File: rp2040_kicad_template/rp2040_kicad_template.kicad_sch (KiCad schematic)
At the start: 48 parts

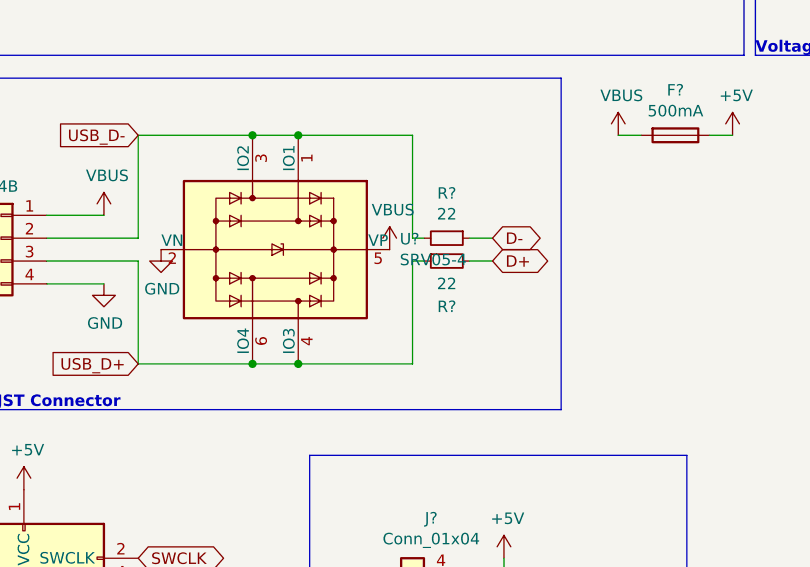
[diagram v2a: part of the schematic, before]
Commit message: Update RP2040 to use 27 ohm resistors
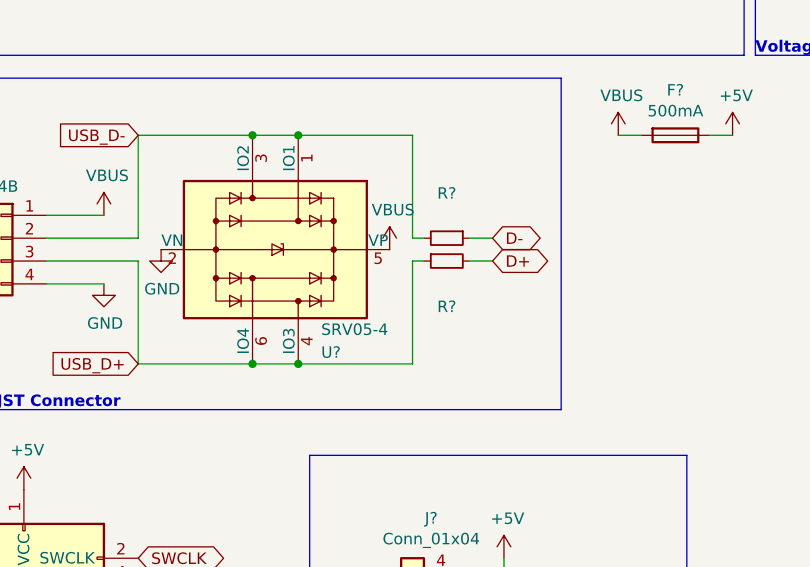
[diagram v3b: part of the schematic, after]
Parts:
- C? (x14), CS?: footprint (none) -> Capacitor_SMD:C_0402_1005Metric
- J?: footprint (none) -> Type-C:USB_C_GCT_USB4085
- R? (x9), RS?: footprint (none) -> Resistor_SMD:R_0402_1005Metric
- R? (x2): value 22 -> (none); footprint (none) -> Resistor_SMD:R_0402_1005Metric
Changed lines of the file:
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@@
     (property "Reference" "R?" (id 0) (at 107.95 34.3916 90))
     (property "Value" "27" (id 1) (at 107.95 36.703 90))
-    (property "Footprint" "" (id 2) (at 107.95 39.37 0)
+    (property "Footprint" "Resistor_SMD:R_0402_1005Metric" (id 2) (at 107.95 39.37 0)
       (effects (font (size 1.27 1.27)) hide)
     )
@@
     (property "Reference" "R?" (id 0) (at 107.95 46.99 90))
     (property "Value" "27" (id 1) (at 107.95 44.45 90))
-    (property "Footprint" "" (id 2) (at 107.95 41.91 0)
+    (property "Footprint" "Resistor_SMD:R_0402_1005Metric" (id 2) (at 107.95 41.91 0)
       (effects (font (size 1.27 1.27)) hide)
     )
@@
     (property "Reference" "R?" (id 0) (at 142.24 36.83 90))
     (property "Value" "10k" (id 1) (at 144.78 36.83 90))
-    (property "Footprint" "" (id 2) (at 147.32 36.83 0)
+    (property "Footprint" "Resistor_SMD:R_0402_1005Metric" (id 2) (at 147.32 36.83 0)
       (effects (font (size 1.27 1.27)) hide)
     )
@@
     (property "Reference" "R?" (id 0) (at 143.51 27.94 90))
     (property "Value" "100" (id 1) (at 143.51 30.48 90))
-    (property "Footprint" "" (id 2) (at 143.51 33.02 0)
+    (property "Footprint" "Resistor_SMD:R_0402_1005Metric" (id 2) (at 143.51 33.02 0)
       (effects (font (size 1.27 1.27)) hide)
     )
@@
     (property "Reference" "R?" (id 0) (at 55.9816 53.34 90))
     (property "Value" "5.1k" (id 1) (at 58.293 53.34 90))
-    (property "Footprint" "" (id 2) (at 60.96 53.34 0)
+    (property "Footprint" "Resistor_SMD:R_0402_1005Metric" (id 2) (at 60.96 53.34 0)
       (effects (font (size 1.27 1.27)) hide)
     )
@@
     (property "Reference" "R?" (id 0) (at 63.6016 53.34 90))
     (property "Value" "5.1k" (id 1) (at 65.913 53.34 90))
-    (property "Footprint" "" (id 2) (at 68.58 53.34 0)
+    (property "Footprint" "Resistor_SMD:R_0402_1005Metric" (id 2) (at 68.58 53.34 0)
       (effects (font (size 1.27 1.27)) hide)
     )
@@
     (in_bom yes) (on_board yes)
     (property "Reference" "R?" (id 0) (at 86.36 95.3516 90))
-    (property "Value" "22" (id 1) (at 86.36 97.663 90))
-    (property "Footprint" "" (id 2) (at 86.36 100.33 0)
+    (property "Value" "" (id 1) (at 86.36 97.663 90))
+    (property "Footprint" "Resistor_SMD:R_0402_1005Metric" (id 2) (at 86.36 100.33 0)
       (effects (font (size 1.27 1.27)) hide)
     )
@@
     (in_bom yes) (on_board yes)
     (property "Reference" "R?" (id 0) (at 86.36 107.95 90))
-    (property "Value" "22" (id 1) (at 86.36 105.41 90))
-    (property "Footprint" "" (id 2) (at 86.36 102.87 0)
+    (property "Value" "" (id 1) (at 86.36 105.41 90))
+    (property "Footprint" "Resistor_SMD:R_0402_1005Metric" (id 2) (at 86.36 102.87 0)
       (effects (font (size 1.27 1.27)) hide)
     )
@@
     (property "Reference" "RS?" (id 0) (at 32.9184 67.31 90))
     (property "Value" "1M" (id 1) (at 30.607 67.31 90))
-    (property "Footprint" "" (id 2) (at 27.94 67.31 0)
+    (property "Footprint" "Resistor_SMD:R_0402_1005Metric" (id 2) (at 27.94 67.31 0)
       (effects (font (size 1.27 1.27)) hide)
     )
@@
       (effects (font (size 1.27 1.27)) (justify left))
     )
-    (property "Footprint" "" (id 2) (at 22.86 67.31 0)
+    (property "Footprint" "Capacitor_SMD:C_0402_1005Metric" (id 2) (at 22.86 67.31 0)
       (effects (font (size 1.27 1.27)) hide)
     )
@@
   (symbol (lib_id "Power_Protection:SRV05-4") (at 67.31 101.6 270) (unit 1)
     (in_bom yes) (on_board yes)
-    (property "Reference" "U?" (id 0) (at 81.1276 100.4316 90)
-      (effects (font (size 1.27 1.27)) (justify left))
-    )
-    (property "Value" "SRV05-4" (id 1) (at 81.1276 102.743 90)
+    (property "Reference" "U?" (id 0) (at 72.39 113.03 90)
+      (effects (font (size 1.27 1.27)) (justify left))
+    )
+    (property "Value" "SRV05-4" (id 1) (at 72.39 110.49 90)
       (effects (font (size 1.27 1.27)) (justify left))
     )
@@
     (property "Reference" "R?" (id 0) (at 208.28 52.07 90))
     (property "Value" "10K" (id 1) (at 210.82 52.07 90))
-    (property "Footprint" "" (id 2) (at 213.36 52.07 0)
+    (property "Footprint" "Resistor_SMD:R_0402_1005Metric" (id 2) (at 213.36 52.07 0)
       (effects (font (size 1.27 1.27)) hide)
     )
@@
     (property "Reference" "R?" (id 0) (at 204.47 83.82 90))
     (property "Value" "1k" (id 1) (at 204.47 86.36 90))
-    (property "Footprint" "" (id 2) (at 204.47 88.9 0)
+    (property "Footprint" "Resistor_SMD:R_0402_1005Metric" (id 2) (at 204.47 88.9 0)
       (effects (font (size 1.27 1.27)) hide)
     )
@@
       (effects (font (size 1.27 1.27)) (justify left))
     )
-    (property "Footprint" "" (id 2) (at 184.15 81.28 0)
+    (property "Footprint" "Capacitor_SMD:C_0402_1005Metric" (id 2) (at 184.15 81.28 0)
       (effects (font (size 1.27 1.27)) hide)
     )
@@
       (effects (font (size 1.27 1.27)) (justify left))
     )
-    (property "Footprint" "" (id 2) (at 184.15 88.9 0)
+    (property "Footprint" "Capacitor_SMD:C_0402_1005Metric" (id 2) (at 184.15 88.9 0)
       (effects (font (size 1.27 1.27)) hide)
     )
@@
       (effects (font (size 1.27 1.27)) (justify left))
     )
-    (property "Footprint" "" (id 2) (at 262.89 22.86 0)
+    (property "Footprint" "Capacitor_SMD:C_0402_1005Metric" (id 2) (at 262.89 22.86 0)
       (effects (font (size 1.27 1.27)) hide)
     )
@@
       (effects (font (size 1.27 1.27)) (justify left))
     )
-    (property "Footprint" "" (id 2) (at 273.05 22.86 0)
+    (property "Footprint" "Capacitor_SMD:C_0402_1005Metric" (id 2) (at 273.05 22.86 0)
       (effects (font (size 1.27 1.27)) hide)
     )
@@
       (effects (font (size 1.27 1.27)) (justify left))
     )
-    (property "Footprint" "" (id 2) (at 283.21 22.86 0)
+    (property "Footprint" "Capacitor_SMD:C_0402_1005Metric" (id 2) (at 283.21 22.86 0)
       (effects (font (size 1.27 1.27)) hide)
     )
@@
       (effects (font (size 1.27 1.27)) (justify left))
     )
-    (property "Footprint" "" (id 2) (at 293.37 22.86 0)
+    (property "Footprint" "Capacitor_SMD:C_0402_1005Metric" (id 2) (at 293.37 22.86 0)
       (effects (font (size 1.27 1.27)) hide)
     )
@@
       (effects (font (size 1.27 1.27)) (justify left))
     )
-    (property "Footprint" "" (id 2) (at 303.53 22.86 0)
+    (property "Footprint" "Capacitor_SMD:C_0402_1005Metric" (id 2) (at 303.53 22.86 0)
       (effects (font (size 1.27 1.27)) hide)
     )
@@
       (effects (font (size 1.27 1.27)) (justify left))
     )
-    (property "Footprint" "" (id 2) (at 313.69 22.86 0)
+    (property "Footprint" "Capacitor_SMD:C_0402_1005Metric" (id 2) (at 313.69 22.86 0)
       (effects (font (size 1.27 1.27)) hide)
     )
@@
       (effects (font (size 1.27 1.27)) (justify left))
     )
-    (property "Footprint" "" (id 2) (at 323.85 22.86 0)
+    (property "Footprint" "Capacitor_SMD:C_0402_1005Metric" (id 2) (at 323.85 22.86 0)
       (effects (font (size 1.27 1.27)) hide)
     )
@@
       (effects (font (size 1.27 1.27)) (justify left))
     )
-    (property "Footprint" "" (id 2) (at 334.01 22.86 0)
+    (property "Footprint" "Capacitor_SMD:C_0402_1005Metric" (id 2) (at 334.01 22.86 0)
       (effects (font (size 1.27 1.27)) hide)
     )
@@
       (effects (font (size 1.27 1.27)) (justify left))
     )
-    (property "Footprint" "" (id 2) (at 344.17 22.86 0)
+    (property "Footprint" "Capacitor_SMD:C_0402_1005Metric" (id 2) (at 344.17 22.86 0)
       (effects (font (size 1.27 1.27)) hide)
     )
@@
       (effects (font (size 1.27 1.27)) (justify left))
     )
-    (property "Footprint" "" (id 2) (at 179.07 22.86 0)
+    (property "Footprint" "Capacitor_SMD:C_0402_1005Metric" (id 2) (at 179.07 22.86 0)
       (effects (font (size 1.27 1.27)) hide)
     )
@@
       (effects (font (size 1.27 1.27)) (justify left))
     )
-    (property "Footprint" "" (id 2) (at 189.23 22.86 0)
+    (property "Footprint" "Capacitor_SMD:C_0402_1005Metric" (id 2) (at 189.23 22.86 0)
       (effects (font (size 1.27 1.27)) hide)
     )
@@
       (effects (font (size 1.27 1.27)) (justify left))
     )
-    (property "Footprint" "" (id 2) (at 240.03 170.18 0)
+    (property "Footprint" "Capacitor_SMD:C_0402_1005Metric" (id 2) (at 240.03 170.18 0)
       (effects (font (size 1.27 1.27)) hide)
     )
@@
     (property "Reference" "J?" (id 0) (at 33.02 17.8902 0))
     (property "Value" "USB_C_Receptacle_USB2.0" (id 1) (at 33.02 20.4271 0))
-    (property "Footprint" "" (id 2) (at 36.83 39.37 0)
+    (property "Footprint" "Type-C:USB_C_GCT_USB4085" (id 2) (at 36.83 39.37 0)
       (effects (font (size 1.27 1.27)) hide)
     )
@@
     (property "Reference" "R?" (id 0) (at 290.83 163.83 90))
     (property "Value" "10K" (id 1) (at 293.37 163.83 90))
-    (property "Footprint" "" (id 2) (at 295.91 163.83 0)
+    (property "Footprint" "Resistor_SMD:R_0402_1005Metric" (id 2) (at 295.91 163.83 0)
       (effects (font (size 1.27 1.27)) hide)
     )
@@
     )
     (path "/00000000-0000-0000-0000-00005e898ff7"
-      (reference "R?") (unit 1) (value "22") (footprint "Resistor_SMD:R_0402_1005Metric")
+      (reference "R?") (unit 1) (value "27") (footprint "Resistor_SMD:R_0402_1005Metric")
     )
     (path "/00000000-0000-0000-0000-00005e898ffd"
-      (reference "R?") (unit 1) (value "22") (footprint "Resistor_SMD:R_0402_1005Metric")
+      (reference "R?") (unit 1) (value "27") (footprint "Resistor_SMD:R_0402_1005Metric")
     )
     (path "/00000000-0000-0000-0000-0000622f92ea"
